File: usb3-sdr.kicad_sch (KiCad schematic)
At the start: 9 parts, among them J1 BNC IN, Q1 BSS84, U1 TCA6408ARGT, U2 SC18IS606PW

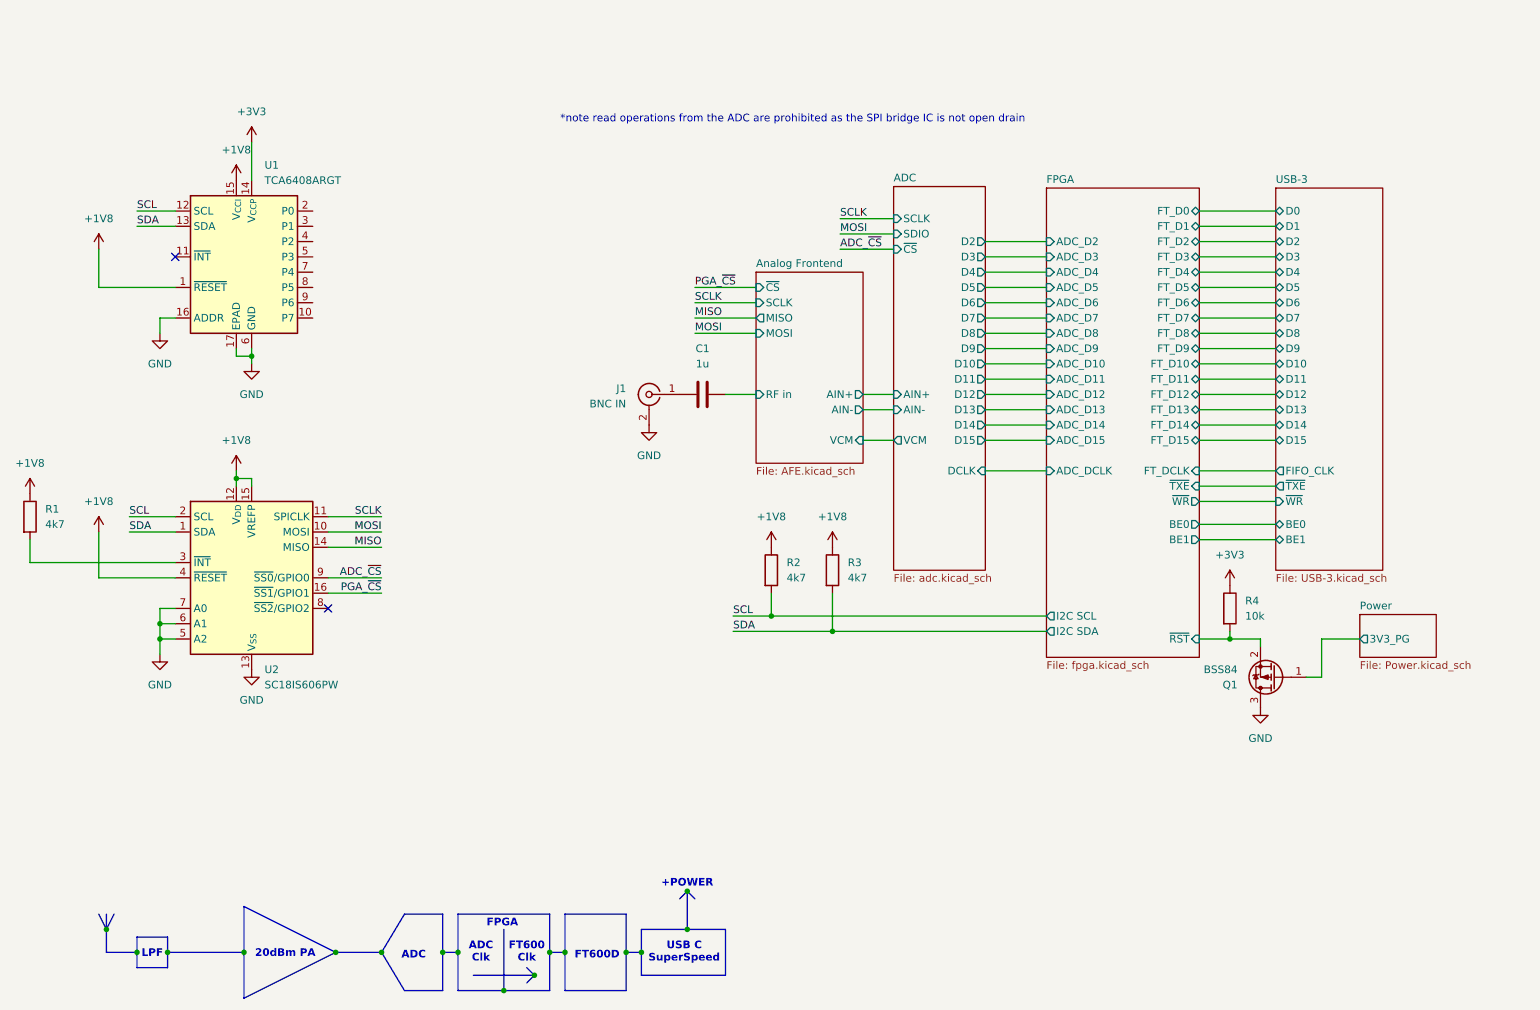
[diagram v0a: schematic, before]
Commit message: Add footprints, fix voltage mismatches, add i2c bus to FT600
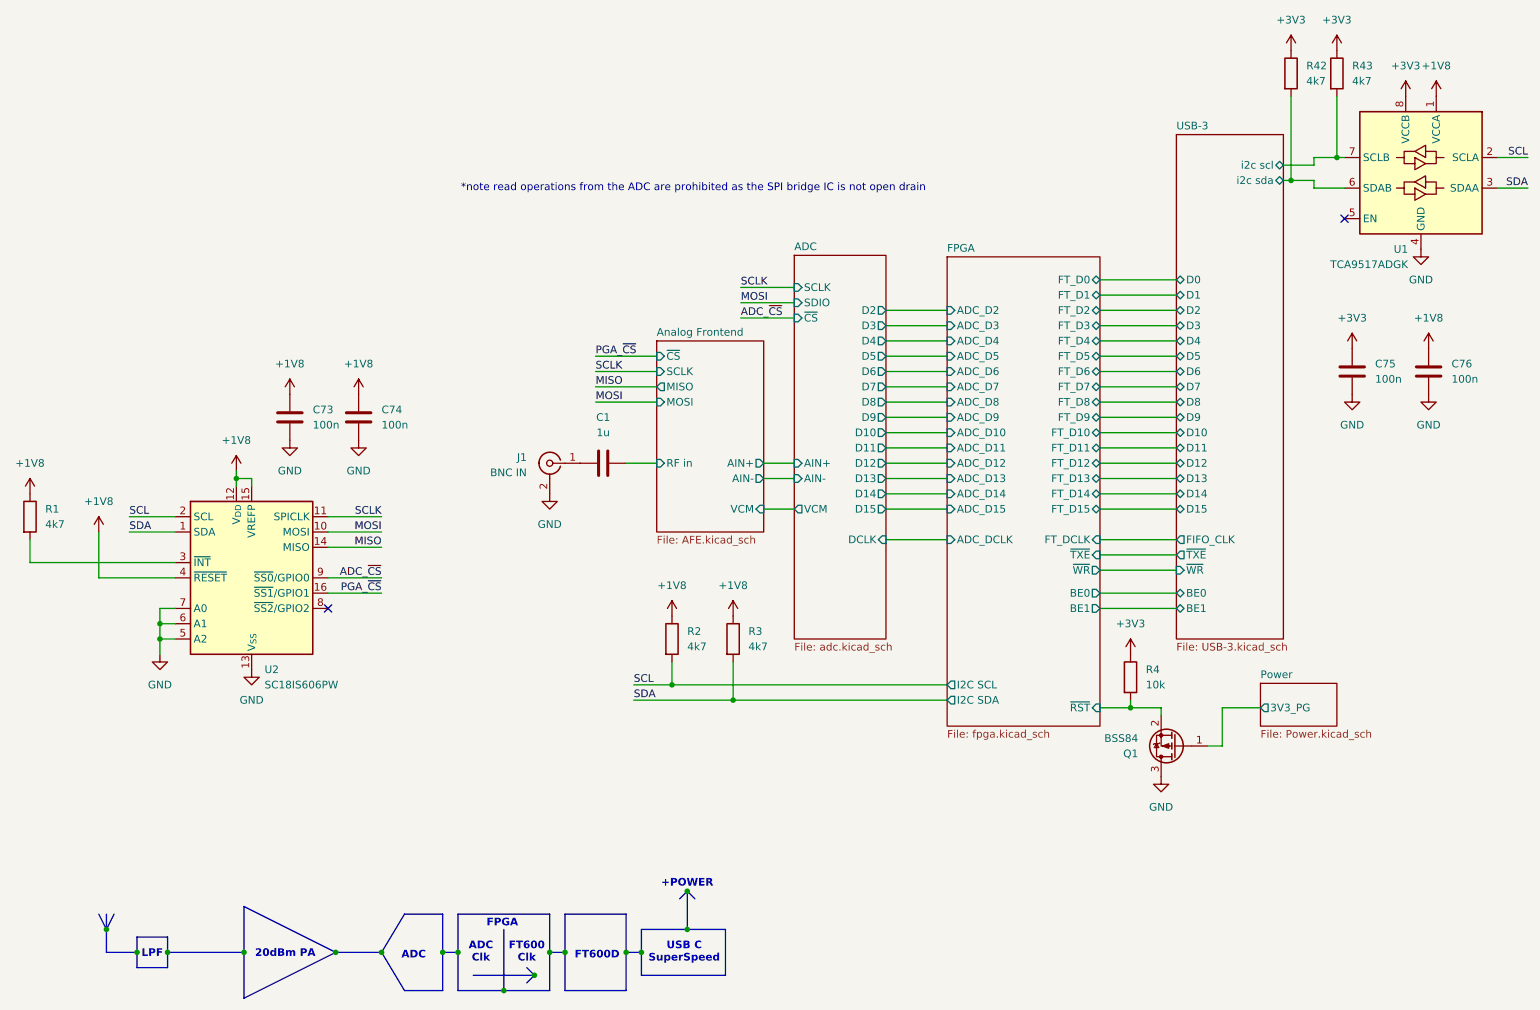
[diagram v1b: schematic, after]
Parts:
- removed U1: TCA6408ARGT, Package_DFN_QFN:VQFN-16-1EP_3x3mm_P0.5mm_EP1.45x1.45mm, symbol Interface_Expansion:TCA6408ARGT
- added C73, C74, C75, C76: 100n, Capacitor_SMD:C_0603_1608Metric, symbol Device:C
- added R42, R43: 4k7, Resistor_SMD:R_0603_1608Metric, symbol Device:R
- added U1: TCA9517ADGK, Package_SO:VSSOP-8_3x3mm_P0.65mm, symbol Logic_LevelTranslator:TCA9517ADGK
- J1: footprint (none) -> plib:BNC-TH_DOSIN-801-0051
- U2: lcsc_id (none) -> C5190384
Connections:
- net +1V8: now also C73.1, C74.1, C76.1, U1.1 (VCCA)
- net +3V3: now also C75.1, R42.1, R43.1, U1.8 (VCCB)
- net GND: now also C73.2, C74.2, C75.2, C76.2, U1.4 (GND)
- net SCL: now also U1.2 (SCLA)
- net SDA: now also U1.3 (SDAA)
- new net USB-3/i2c scl: R43.2, U1.7 (SCLB)
- new net USB-3/i2c sda: R42.2, U1.6 (SDAB)
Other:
- sheet USB-3 ports: added i2c scl, i2c sda; removed none
- moved on the sheet: C1, J1, Q1, R2, R3, R4

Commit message: Fix ferrite, etc
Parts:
- renumbered C73 to C1, C74 to C2, C1 to C3, C75 to C4, C76 to C5, R42 to R5, R43 to R6, U2 to U1, U1 to U2
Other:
- note added: "VGA"
- note removed: "20dBm PA"
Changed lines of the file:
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@@
 	(text "FT600D"
 		(exclude_from_sim no)
-		(at 123.444 170.688 0)
+		(at 123.19 170.434 0)
 		(effects
 			(font
@@
 		)
 	)
-	(text "20dBm PA"
+	(text "VGA"
 		(exclude_from_sim no)
 		(at 71.628 170.434 0)
@@
 		(dnp no)
 		(fields_autoplaced yes)
-		(property "Reference" "C74"
+		(property "Reference" "C2"
 			(at 87.63 80.0099 0)
 			(effects
@@
 			(project "usb3-sdr"
 				(path "/c130ee0c-52ab-4414-8ea8-abd1a940c0be"
-					(reference "C74")
+					(reference "C2")
 					(unit 1)
 				)
@@
 		(dnp no)
 		(fields_autoplaced yes)
-		(property "Reference" "#PWR09"
+		(property "Reference" "#PWR020"
 			(at 260.35 59.69 0)
 			(effects
@@
 			(project ""
 				(path "/c130ee0c-52ab-4414-8ea8-abd1a940c0be"
-					(reference "#PWR09")
+					(reference "#PWR020")
 					(unit 1)
 				)
@@
 		(dnp no)
 		(fields_autoplaced yes)
-		(property "Reference" "#PWR05"
+		(property "Reference" "#PWR03"
 			(at 50.8 127 0)
 			(effects
@@
 			(project ""
 				(path "/c130ee0c-52ab-4414-8ea8-abd1a940c0be"
-					(reference "#PWR05")
+					(reference "#PWR03")
 					(unit 1)
 				)
@@
 		(on_board yes)
 		(dnp no)
-		(property "Reference" "U1"
+		(property "Reference" "U2"
 			(at 258.2067 53.34 0)
 			(effects
@@
 			(project ""
 				(path "/c130ee0c-52ab-4414-8ea8-abd1a940c0be"
-					(reference "U1")
+					(reference "U2")
 					(unit 1)
 				)
@@
 		(dnp no)
 		(fields_autoplaced yes)
-		(property "Reference" "C1"
+		(property "Reference" "C3"
 			(at 124.46 81.28 90)
 			(effects
@@
 			(project "usb3-sdr"
 				(path "/c130ee0c-52ab-4414-8ea8-abd1a940c0be"
-					(reference "C1")
+					(reference "C3")
 					(unit 1)
 				)
@@
 		(dnp no)
 		(fields_autoplaced yes)
-		(property "Reference" "#PWR010"
+		(property "Reference" "#PWR05"
 			(at 66.04 129.54 0)
 			(effects
@@
 			(project ""
 				(path "/c130ee0c-52ab-4414-8ea8-abd1a940c0be"
-					(reference "#PWR010")
+					(reference "#PWR05")
 					(unit 1)
 				)
@@
 		(dnp no)
 		(fields_autoplaced yes)
-		(property "Reference" "#PWR0160"
+		(property "Reference" "#PWR021"
 			(at 261.62 73.66 0)
 			(effects
@@
 			(project "usb3-sdr"
 				(path "/c130ee0c-52ab-4414-8ea8-abd1a940c0be"
-					(reference "#PWR0160")
+					(reference "#PWR021")
 					(unit 1)
 				)
@@
 		(dnp no)
 		(fields_autoplaced yes)
-		(property "Reference" "#PWR07"
+		(property "Reference" "#PWR04"
 			(at 63.5 93.98 0)
 			(effects
@@
 			(project ""
 				(path "/c130ee0c-52ab-4414-8ea8-abd1a940c0be"
-					(reference "#PWR07")
+					(reference "#PWR04")
 					(unit 1)
 				)
@@
 		(dnp no)
 		(fields_autoplaced yes)
-		(property "Reference" "#PWR014"
+		(property "Reference" "#PWR013"
 			(at 212.09 124.46 0)
 			(effects
@@
 			(project "usb3-sdr"
 				(path "/c130ee0c-52ab-4414-8ea8-abd1a940c0be"
-					(reference "#PWR014")
+					(reference "#PWR013")
 					(unit 1)
 				)
@@
 		(dnp no)
 		(fields_autoplaced yes)
-		(property "Reference" "#PWR013"
+		(property "Reference" "#PWR012"
 			(at 146.05 118.11 0)
 			(effects
@@
 			(project ""
 				(path "/c130ee0c-52ab-4414-8ea8-abd1a940c0be"
-					(reference "#PWR013")
+					(reference "#PWR012")
 					(unit 1)
 				)
@@
 		(dnp no)
 		(fields_autoplaced yes)
-		(property "Reference" "#PWR04"
+		(property "Reference" "#PWR08"
 			(at 83.82 81.28 0)
 			(effects
@@
 			(project "usb3-sdr"
 				(path "/c130ee0c-52ab-4414-8ea8-abd1a940c0be"
-					(reference "#PWR04")
+					(reference "#PWR08")
 					(unit 1)
 				)
@@
 		(dnp no)
 		(fields_autoplaced yes)
-		(property "Reference" "#PWR0157"
+		(property "Reference" "#PWR019"
 			(at 257.81 31.75 0)
 			(effects
@@
 			(project ""
 				(path "/c130ee0c-52ab-4414-8ea8-abd1a940c0be"
-					(reference "#PWR0157")
+					(reference "#PWR019")
 					(unit 1)
 				)
@@
 		(dnp no)
 		(fields_autoplaced yes)
-		(property "Reference" "R43"
+		(property "Reference" "R6"
 			(at 248.92 22.8599 0)
 			(effects
@@
 			(project "usb3-sdr"
 				(path "/c130ee0c-52ab-4414-8ea8-abd1a940c0be"
-					(reference "R43")
+					(reference "R6")
 					(unit 1)
 				)
@@
 		(dnp no)
 		(fields_autoplaced yes)
-		(property "Reference" "#PWR0156"
+		(property "Reference" "#PWR015"
 			(at 238.76 24.13 0)
 			(effects
@@
 			(project "usb3-sdr"
 				(path "/c130ee0c-52ab-4414-8ea8-abd1a940c0be"
-					(reference "#PWR0156")
+					(reference "#PWR015")
 					(unit 1)
 				)
@@
 		(dnp no)
 		(fields_autoplaced yes)
-		(property "Reference" "#PWR011"
+		(property "Reference" "#PWR010"
 			(at 115.57 100.33 0)
 			(effects
@@
 			(project "usb3-sdr"
 				(path "/c130ee0c-52ab-4414-8ea8-abd1a940c0be"
-					(reference "#PWR011")
+					(reference "#PWR010")
 					(unit 1)
 				)
@@
 		(dnp no)
 		(fields_autoplaced yes)
-		(property "Reference" "#PWR08"
+		(property "Reference" "#PWR09"
 			(at 83.82 91.44 0)
 			(effects
@@
 			(project "usb3-sdr"
 				(path "/c130ee0c-52ab-4414-8ea8-abd1a940c0be"
-					(reference "#PWR08")
+					(reference "#PWR09")
 					(unit 1)
 				)
@@
 		(dnp no)
 		(fields_autoplaced yes)
-		(property "Reference" "#PWR012"
+		(property "Reference" "#PWR011"
 			(at 135.89 118.11 0)
 			(effects
@@
 			(project "usb3-sdr"
 				(path "/c130ee0c-52ab-4414-8ea8-abd1a940c0be"
-					(reference "#PWR012")
+					(reference "#PWR011")
 					(unit 1)
 				)
@@
 		(dnp no)
 		(fields_autoplaced yes)
-		(property "Reference" "C76"
+		(property "Reference" "C5"
 			(at 265.43 72.3899 0)
 			(effects
@@
 			(project "usb3-sdr"
 				(path "/c130ee0c-52ab-4414-8ea8-abd1a940c0be"
-					(reference "C76")
+					(reference "C5")
 					(unit 1)
 				)
@@
 		(dnp no)
 		(fields_autoplaced yes)
-		(property "Reference" "#PWR015"
+		(property "Reference" "#PWR014"
 			(at 217.17 147.32 0)
 			(effects
@@
 			(project ""
 				(path "/c130ee0c-52ab-4414-8ea8-abd1a940c0be"
-					(reference "#PWR015")
+					(reference "#PWR014")
 					(unit 1)
 				)
@@
 		(dnp no)
 		(fields_autoplaced yes)
-		(property "Reference" "#PWR06"
+		(property "Reference" "#PWR07"
 			(at 72.39 91.44 0)
 			(effects
@@
 			(project ""
 				(path "/c130ee0c-52ab-4414-8ea8-abd1a940c0be"
-					(reference "#PWR06")
+					(reference "#PWR07")
 					(unit 1)
 				)
@@
 		(dnp no)
 		(fields_autoplaced yes)
-		(property "Reference" "C75"
+		(property "Reference" "C4"
 			(at 252.73 72.3899 0)
 			(effects
@@
 			(project ""
 				(path "/c130ee0c-52ab-4414-8ea8-abd1a940c0be"
-					(reference "C75")
+					(reference "C4")
 					(unit 1)
 				)
@@
 		(dnp no)
 		(fields_autoplaced yes)
-		(property "Reference" "#PWR0162"
+		(property "Reference" "#PWR022"
 			(at 261.62 83.82 0)
 			(effects
@@
 			(project "usb3-sdr"
 				(path "/c130ee0c-52ab-4414-8ea8-abd1a940c0be"
-					(reference "#PWR0162")
+					(reference "#PWR022")
 					(unit 1)
 				)
@@
 		(dnp no)
 		(fields_autoplaced yes)
-		(property "Reference" "U2"
+		(property "Reference" "U1"
 			(at 68.1833 123.19 0)
 			(effects
@@
 			(project ""
 				(path "/c130ee0c-52ab-4414-8ea8-abd1a940c0be"
-					(reference "U2")
+					(reference "U1")
 					(unit 1)
 				)
@@
 		(dnp no)
 		(fields_autoplaced yes)
-		(property "Reference" "#PWR0159"
+		(property "Reference" "#PWR017"
 			(at 248.92 73.66 0)
 			(effects
@@
 			(project "usb3-sdr"
 				(path "/c130ee0c-52ab-4414-8ea8-abd1a940c0be"
-					(reference "#PWR0159")
+					(reference "#PWR017")
 					(unit 1)
 				)
@@
 		(dnp no)
 		(fields_autoplaced yes)
-		(property "Reference" "#PWR02"
+		(property "Reference" "#PWR06"
 			(at 72.39 81.28 0)
 			(effects
@@
 			(project "usb3-sdr"
 				(path "/c130ee0c-52ab-4414-8ea8-abd1a940c0be"
-					(reference "#PWR02")
+					(reference "#PWR06")
 					(unit 1)
 				)
@@
 		(dnp no)
 		(fields_autoplaced yes)
-		(property "Reference" "R42"
+		(property "Reference" "R5"
 			(at 241.3 22.8599 0)
 			(effects
@@
 			(project ""
 				(path "/c130ee0c-52ab-4414-8ea8-abd1a940c0be"
-					(reference "R42")
+					(reference "R5")
 					(unit 1)
 				)
@@
 		(dnp no)
 		(fields_autoplaced yes)
-		(property "Reference" "#PWR03"
+		(property "Reference" "#PWR02"
 			(at 40.64 104.14 0)
 			(effects
@@
 			(project "usb3-sdr"
 				(path "/c130ee0c-52ab-4414-8ea8-abd1a940c0be"
-					(reference "#PWR03")
+					(reference "#PWR02")
 					(unit 1)
 				)
@@
 		(dnp no)
 		(fields_autoplaced yes)
-		(property "Reference" "#PWR0155"
+		(property "Reference" "#PWR016"
 			(at 246.38 24.13 0)
 			(effects
@@
 			(project ""
 				(path "/c130ee0c-52ab-4414-8ea8-abd1a940c0be"
-					(reference "#PWR0155")
+					(reference "#PWR016")
 					(unit 1)
 				)
@@
 		(dnp no)
 		(fields_autoplaced yes)
-		(property "Reference" "#PWR0158"
+		(property "Reference" "#PWR023"
 			(at 262.89 31.75 0)
 			(effects
@@
 			(project ""
 				(path "/c130ee0c-52ab-4414-8ea8-abd1a940c0be"
-					(reference "#PWR0158")
+					(reference "#PWR023")
 					(unit 1)
 				)
@@
 		(dnp no)
 		(fields_autoplaced yes)
-		(property "Reference" "#PWR0161"
+		(property "Reference" "#PWR018"
 			(at 248.92 83.82 0)
 			(effects
@@
 			(project ""
 				(path "/c130ee0c-52ab-4414-8ea8-abd1a940c0be"
-					(reference "#PWR0161")
+					(reference "#PWR018")
 					(unit 1)
 				)
@@
 		(dnp no)
 		(fields_autoplaced yes)
-		(property "Reference" "C73"
+		(property "Reference" "C1"
 			(at 76.2 80.0099 0)
 			(effects
@@
 			(project ""
 				(path "/c130ee0c-52ab-4414-8ea8-abd1a940c0be"
-					(reference "C73")
+					(reference "C1")
 					(unit 1)
 				)
